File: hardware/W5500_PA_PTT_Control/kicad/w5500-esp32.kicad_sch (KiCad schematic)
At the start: 22 parts, among them J1 ESP32_DevKitC_Socket_40P_25.4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, J2 DC_IN_13V8, J5 Power, J6 PTT_ON, Q1 2SC1815, Q3 2SC1815, Q5 2SJ334, U1 TA48033S, U2 L7805

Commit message: W5500 PA/PTT制御基板の回路図でR8を1kから100に変更
Co-Authored-By: Claude Opus 5.5 <noreply@anthropic.com>
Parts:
- R8: value 1k -> 100
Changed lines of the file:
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@@
 			)
 		)
-		(property "Value" "1k"
+		(property "Value" "100"
 			(at 313.69 63.5 90)
 			(show_name no)

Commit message: W5500制御基板: R8を1kΩに、R12(Q1ベースのプルダウン)追加、Q5の足番号修正、放熱器を追加
- R8(Q5ゲートのプルアップ)を100Ωから1kΩ(1/2W推奨)へ。Q1 ON中の電流を約12〜14mAに抑える
- Q1のベースをGNDへプルダウンするR12(10kΩ)を追加(GPIO26が確定しない間もQ1をOFFに保つ)
- Q5のシンボルを端子番号1=G・2=D・3=Sのproject_symbols:2SJ334に変更
  (従来のDevice:Q_PMOSは端子番号D/G/Sで、基板データ上Q5が未接続になっていた)
- U1・U2・Q5に放熱器(秋月[105054] 20×20×25mm)。基板データでTO-220の3部品を25mm間隔に配置
- 仕様書(Rev.2.4)・接続一覧(日英・Word・PDF)、回路図PDF/SVGを更新
- ERCの件数は変更前と同じ(15件)。DRCの回路図一致チェックでR8の値とQ5のパッド未接続が解消

Co-Authored-By: Claude Opus 5.5 <noreply@anthropic.com>
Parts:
- added R12: 10k, Resistor_THT:R_Axial_DIN0207_L6.3mm_D2.5mm_P5.08mm_Vertical, symbol Device:R
- Q5: symbol Device:Q_PMOS -> project_symbols:2SJ334
- R8: value 100 -> 1k
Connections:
- net +12V: now also Q5.3 (S); no longer Q5.S
- net Power: now also Q5.2 (D); no longer Q5.D
- net at Q1.2 (C), R8.1: now also Q5.1 (G); no longer Q5.G
- net at Q1.3 (B), R6.2: now also R12.1
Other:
- note added: "U2: 13.8V(+12V)を5VへLDO変換(L7805)。発熱(13.8V-5V)*0.2A=約1.76Wのため放熱器を使用。 U1: 上記5VをさらにW5500(A1)専用の+3V3_Aへ変換(TA48033S)。発熱(5V-3.3V)*0.2A=約0.34W。放熱器を使用。 放熱器: U1・U2・Q5とも秋月[105054] 20×20×25mm(20PB020-01025、15.8℃/W)。 ESP32側(J1の3V3、DevKitC基板のオンボードLDO経由)とは完全に独立した系統。"
- note removed: "U2: 13.8V(+12V)を5VへLDO変換(L7805)。発熱(13.8V-5V)*0.2A=約1.76Wのためヒートシンク推奨。 U1: 上記5VをさらにW5500(A1)専用の+3V3_Aへ変換(TA48033S)。発熱(5V-3.3V)*0.2A=約0.34W。 ESP32側(J1の3V3、DevKitC基板のオンボードLDO経由)とは完全に独立した系統。"
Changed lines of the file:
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@@
 		)
 	)
-	(text "U2: 13.8V(+12V)を5VへLDO変換(L7805)。発熱(13.8V-5V)*0.2A=約1.76Wのためヒートシンク推奨。\nU1: 上記5VをさらにW5500(A1)専用の+3V3_Aへ変換(TA48033S)。発熱(5V-3.3V)*0.2A=約0.34W。\nESP32側(J1の3V3、DevKitC基板のオンボードLDO経由)とは完全に独立した系統。"
+	(text "U2: 13.8V(+12V)を5VへLDO変換(L7805)。発熱(13.8V-5V)*0.2A=約1.76Wのため放熱器を使用。\nU1: 上記5VをさらにW5500(A1)専用の+3V3_Aへ変換(TA48033S)。発熱(5V-3.3V)*0.2A=約0.34W。放熱器を使用。\n放熱器: U1・U2・Q5とも秋月[105054] 20×20×25mm(20PB020-01025、15.8℃/W)。\nESP32側(J1の3V3、DevKitC基板のオンボードLDO経由)とは完全に独立した系統。"
 		(exclude_from_sim no)
 		(at 256.794 139.954 0)
@@
 	)
 	(symbol
-		(lib_id "Device:Q_PMOS")
+		(lib_id "project_symbols:2SJ334")
 		(at 322.58 58.42 270)
 		(mirror x)
@@
 			)
 		)
-		(pin "D"
+		(pin "2"
 		)
-		(pin "G"
+		(pin "1"
 		)
-		(pin "S"
+		(pin "3"
 		)
 		(instances
@@
 			)
 		)
-		(property "Value" "100"
+		(property "Value" "1k"
 			(at 313.69 63.5 90)
 			(show_name no)
@@
 					(unit 1)
 				)
+			)
+		)
+	)
+	(wire
+		(pts
+			(xy 309.88 90.17) (xy 309.88 91.44)
+		)
+		(stroke
+			(width 0)
+			(type default)
+		)
+	)
+	(junction
+		(at 309.88 90.17)
+		(diameter 0)
+		(color 0 0 0 0)
+	)
+	(symbol
+		(lib_id "Device:R")
+		(at 309.88 95.25 0)
+		(unit 1)
+		(body_style 1)
+		(exclude_from_sim no)
+		(in_bom yes)
+		(on_board yes)
+		(in_pos_files yes)
+		(dnp no)
+		(property "Reference" "R12"
+			(at 311.912 94.0 0)
+			(show_name no)
+			(do_not_autoplace no)
+			(effects
+				(font
+					(size 1.27 1.27)
+				)
+			)
+		)
+		(property "Value" "10k"
+			(at 311.912 96.52 0)
+			(show_name no)
+			(do_not_autoplace no)
+			(effects
+				(font
+					(size 1.27 1.27)
+				)
+			)
+		)
+		(property "Footprint" "Resistor_THT:R_Axial_DIN0207_L6.3mm_D2.5mm_P5.08mm_Vertical"
+			(at 308.102 95.25 90)
+			(hide yes)
+			(show_name yes)
+			(do_not_autoplace no)
+			(effects
+				(font
+					(size 1.27 1.27)
+				)
+			)
+		)
+		(property "Datasheet" ""
+			(at 309.88 95.25 0)
+			(hide yes)
+			(show_name yes)
+			(do_not_autoplace no)
+			(effects
+				(font
+					(size 1.27 1.27)
+				)
+			)
+		)
+		(property "Description" ""
+			(at 309.88 95.25 0)
+			(hide yes)
+			(show_name yes)
+			(do_not_autoplace no)
+			(effects
+				(font
+					(size 1.27 1.27)
+				)
+			)
+		)
+		(pin "1"
+		)
+		(pin "2"
+		)
+		(instances
+			(project "w5500-esp32"
+				(path "/0100d23c-65ba-4b48-9527-fff8f2d69db1"
+					(reference "R12")
+					(unit 1)
+				)
+			)
+		)
+	)
+	(symbol
+		(lib_id "power:GND")
+		(at 309.88 99.06 0)
+		(unit 1)
+		(body_style 1)
+		(exclude_from_sim no)
+		(in_bom yes)
+		(on_board yes)
+		(in_pos_files yes)
+		(dnp no)
+		(fields_autoplaced yes)
+		(property "Reference" "#PWR0301"
+			(at 309.88 105.41 0)
+			(hide yes)
+			(show_name yes)
+			(do_not_autoplace no)
+			(effects
+				(font
+					(size 1.27 1.27)
+				)
+			)
+		)
+		(property "Value" ""
+			(at 322.58 102.87 0)
+			(show_name no)
+			(do_not_autoplace no)
+			(effects
+				(font
+					(size 1.27 1.27)
+				)
+			)
+		)
+		(property "Footprint" ""
+			(at 322.58 97.79 0)
+			(hide yes)
+			(show_name yes)
+			(do_not_autoplace no)
+			(effects
+				(font
+					(size 1.27 1.27)
+				)
+			)
+		)
+		(property "Datasheet" ""
+			(at 322.58 97.79 0)
+			(hide yes)
+			(show_name yes)
+			(do_not_autoplace no)
+			(effects
+				(font
+					(size 1.27 1.27)
+				)
+			)
+		)
+		(property "Description" "Power symbol creates a global label with name \"GND\" , ground"
+			(at 322.58 97.79 0)
+			(hide yes)
+			(show_name yes)
+			(do_not_autoplace no)
+			(effects
+				(font
+					(size 1.27 1.27)
+				)
+			)
+		)
+		(pin "1"
+		)
+		(instances
+			(project "w5500-esp32"
+				(path "/0100d23c-65ba-4b48-9527-fff8f2d69db1"
+					(reference "#PWR0301")
+					(unit 1)
+				)

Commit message: W5500とDevKitCのフットプリントを実物の資料に合わせて修正し、ケースの開口に合わせて配置
- A1(W5500 Lite): USR-ES1データシートに合わせ、ピン列間隔を15.24→20.32mm、7〜12番をRJ45側から数える順に修正
  (従来は右列の信号が逆につながる配置だった)。新フットプリントW5500_Lite_USR-ES1_2x06_P2.54mm_20.32mm
- J1(DevKitCソケット): Freenove公式ピン配置図に合わせ、ピンの並びを上下反転(1番5V・21番GNDがUSB-C側)。
  従来は鏡像の並びで、5Vが3V3/GNDのピンにつながる配置だった
- RJ45をケース前面の角穴(基板x=122)、USB-Cを背面の角丸穴(x=126)に合わせて配置
- 接続一覧(日英・Word・PDF)に修正内容を追記、回路図PDF/SVGを再出力。DRC違反0件

Co-Authored-By: Claude Opus 5.5 <noreply@anthropic.com>
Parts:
- A1: footprint project_footprints:W5500_Lite_2x06_P2.54mm_15.24mm -> project_footprints:W5500_Lite_USR-ES1_2x06_P2.54mm_20.32mm
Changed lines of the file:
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@@
 			)
 		)
-		(property "Footprint" "project_footprints:W5500_Lite_2x06_P2.54mm_15.24mm"
+		(property "Footprint" "project_footprints:W5500_Lite_USR-ES1_2x06_P2.54mm_20.32mm"
 			(at 106.68 68.58 0)
 			(hide yes)

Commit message: J2(+12V入力)・J5(12V出力)・J6(PTT出力)を電線はんだ付け用パッドとして配置
- ケースの丸型コネクタ(WTN-11-1253 8P)へ電線でつなぐ前提で、回路図にフットプリントを指定
  (J2・J5: Connector_Wire SolderWire-1sqmm、J6: SolderWire-0.5sqmm)
- J2は前面の丸型コネクタ側(右上)、J5・J6は背面の丸型コネクタ側(右下)に配置
- 「フットプリントが見つからない」3件を解消。DRC違反0件、ERCは変更前と同じ15件
- 仕様書(日英・Word・PDF)の配置説明を更新、回路図PDF/SVGを再出力

Co-Authored-By: Claude Opus 5.5 <noreply@anthropic.com>
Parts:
- J2, J5: footprint (none) -> Connector_Wire:SolderWire-1sqmm_1x02_P5.4mm_D1.4mm_OD2.7mm
- J6: footprint (none) -> Connector_Wire:SolderWire-0.5sqmm_1x02_P4.6mm_D0.9mm_OD2.1mm
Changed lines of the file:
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@@
 			)
 		)
-		(property "Footprint" ""
+		(property "Footprint" "Connector_Wire:SolderWire-1sqmm_1x02_P5.4mm_D1.4mm_OD2.7mm"
 			(at 142.875 171.45 0)
 			(hide yes)
@@
 			)
 		)
-		(property "Footprint" ""
+		(property "Footprint" "Connector_Wire:SolderWire-1sqmm_1x02_P5.4mm_D1.4mm_OD2.7mm"
 			(at 374.65 92.71 0)
 			(hide yes)
@@
 			)
 		)
-		(property "Footprint" ""
+		(property "Footprint" "Connector_Wire:SolderWire-0.5sqmm_1x02_P4.6mm_D0.9mm_OD2.1mm"
 			(at 374.65 113.03 0)
 			(hide yes)

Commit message: W5500制御基板: 自動配線・12V系統強化・外付けLED/XHコネクタ化と総点検の修正
- 回路図のGND記号の値が空で別ネットになっていたのを修正
- 内層をGND・+12Vの全面ベタにし、12V出力(/Power)を表裏4mmで配線、残りをFreeroutingで自動配線
- Q1/Q3を2.54mmピッチのTO-92に、R8を1/2W抵抗用フットプリントに変更
- D1/D2を外付けにしてJ7/J8で接続、J6/J7/J8をJST XH(B2B-XH-A)に変更
- C2をTA48033Sデータシートどおり33µF、C1/C3を0.33µFに変更
- Q3ベースにプルダウンR13(10k)を追加、J1のGNDピン21〜24・40を接続
- 仕様書・接続一覧(日英)を更新しWord/PDF・回路図PDF/SVGを再生成

Co-Authored-By: Claude Opus 5.5 <noreply@anthropic.com>
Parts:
- removed D1: LED_Red_3mm, LED_THT:LED_D3.0mm, symbol Device:LED
- removed D2: LED_Green_3mm, LED_THT:LED_D3.0mm, symbol Device:LED
- added J7: LED_PWR, Connector_JST:JST_XH_B2B-XH-A_1x02_P2.50mm_Vertical, symbol Connector_Generic:Conn_01x02
- added J8: LED_12V, Connector_JST:JST_XH_B2B-XH-A_1x02_P2.50mm_Vertical, symbol Connector_Generic:Conn_01x02
- added R13: 10k, Resistor_THT:R_Axial_DIN0207_L6.3mm_D2.5mm_P5.08mm_Vertical, symbol Device:R
- C1, C3: value 0.1uF -> 0.33uF
- C2: value 0.1uF -> 33uF
- J6: footprint Connector_Wire:SolderWire-0.5sqmm_1x02_P4.6mm_D0.9mm_OD2.1mm -> Connector_JST:JST_XH_B2B-XH-A_1x02_P2.50mm_Vertical
- Q1, Q3: footprint Package_TO_SOT_THT:TO-92_Inline -> Package_TO_SOT_THT:TO-92_Inline_Wide
- R8: footprint Resistor_THT:R_Axial_DIN0207_L6.3mm_D2.5mm_P5.08mm_Vertical -> Resistor_THT:R_Axial_DIN0309_L9.0mm_D3.2mm_P5.08mm_Vertical
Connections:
- net GND: now also C1.2, C2.2, J1.21 (GND), J1.22 (GND), J1.23 (GND), J1.24 (GND), J1.40 (GND), J1.7 (GND), J2.2 (Pin_2), J5.2 (Pin_2), MCU1.7 (GND), Q1.1 (E), Q3.1 (E), R12.2, U1.3 (GND), U2.2 (GND), J7.2 (Pin_2), J8.2 (Pin_2), R13.2
- net at R11.2: now also J8.1 (Pin_1)
- net at R10.2: now also J7.1 (Pin_1)
- net at Q3.3 (B), R7.2: now also R13.1
- no-connect marks 60 -> 55

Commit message: W5500制御基板: +5Vを信号線から離し、J1のピン間に配線を通さないよう再配線、J1の12番ピンを未接続に
- J1の35番ピン(W5500 RST)の配線が+5Vのビアに0.3mmまで近づいていたため、+5V(/+5v0)を
  ネットクラスSupply5V(間隔0.5mm、線幅0.6mm)に分けて再配線した。C1自身の足の間(0.4mm)だけは
  w5500-esp32.kicad_druの例外ルールで0.25mmとする。
- はんだブリッジを避けるため、J1のピンとピンの間に表裏とも配線禁止領域を置いた
  (同じ+5Vの1番・2番の間を除く)。ピン間を突き抜ける配線は0本。
- 回路図でJ1の12番ピン(GPIO25)を未接続(×)にし、MCU1に残っていたGPIO25_LNAラベルを削除した。
- DRC違反0・未配線0。ガーバー・ドリル(スルーホール103穴、ビア4)、回路図PDF/SVG、仕様書・接続一覧を更新した。

Co-Authored-By: Claude Opus 5.5 <noreply@anthropic.com>
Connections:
- net GPIO25_LNA: no longer names the net of MCU1.12 (GPIO25)
- no-connect marks 55 -> 57
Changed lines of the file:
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@@
+	)
+	(no_connect
+		(at 195.58 92.71)
+	)
+	(no_connect
+		(at 64.77 213.36)
 	)
 	(no_connect
@@
 		(pts
 			(xy 295.91 55.88) (xy 307.34 55.88)
-		)
-		(stroke
-			(width 0)
-			(type default)
-		)
-	)
-	(wire
-		(pts
-			(xy 64.77 213.36) (xy 49.53 213.36)
 		)
 		(stroke
@@
 		(effects
 			(font
-				(size 1.27 1.27)
-			)
-		)
-	)
-	(label "GPIO25_LNA"
-		(at 49.53 213.36 0)
-		(effects
-			(font

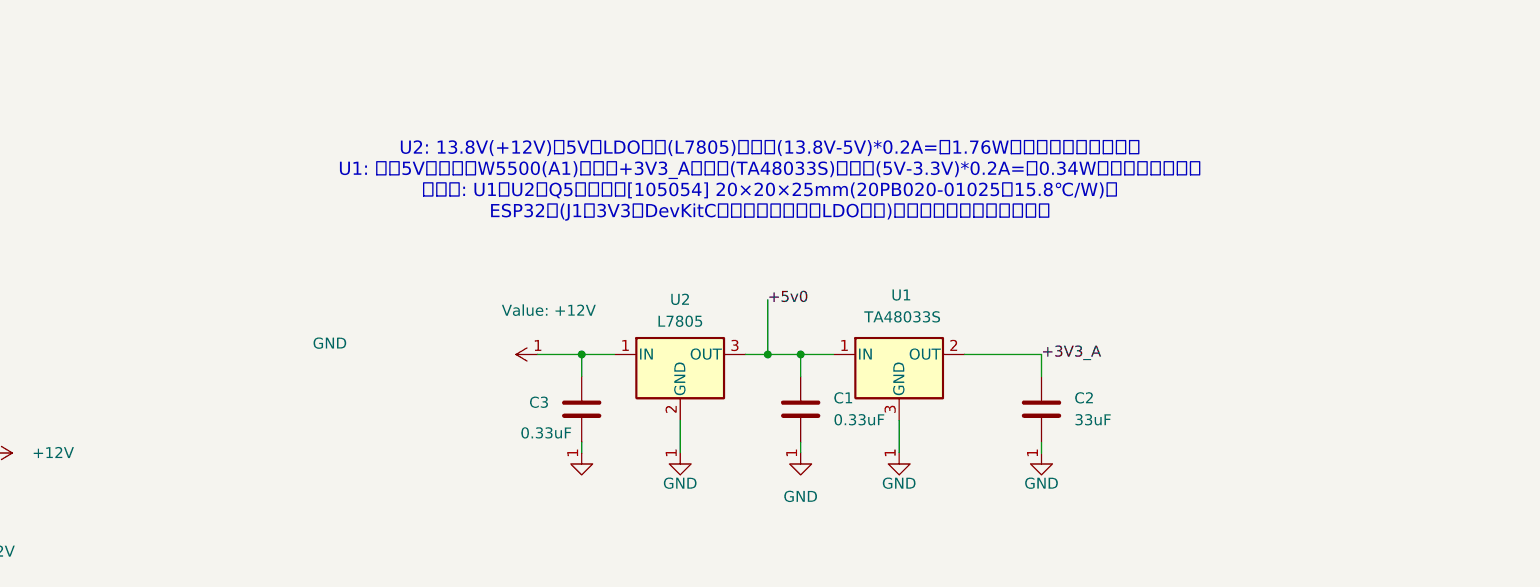
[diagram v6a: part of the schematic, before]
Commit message: W5500制御基板 Rev.1.2: 3.3VレギュレータU1をLM2940T-3.3に変更
- U1をTA48033SからLM2940T-3.3(TO-220、1=IN・2=GND・3=OUT)に変更。足の並びが違うため
  U1の2番をGND、3番を+3V3_Aにつなぎ替え、裏面の+3V3_Aの配線を引き直してベタを再充填
- C1をLM2940のデータシートどおり0.47µFに変更(C2の33µFは22µF以上・ESR 0.1〜1Ωの条件を満たす)
- U1のシンボルをproject_symbolsに追加。DRC違反0・未接続0
- シルクの版数をRev.1.2、仕様書をRev.2.8にし、版数の対応表・接続一覧を更新
- ガーバー・ドリル・ZIP・BOM・README、回路図PDF/SVG、実装図PDF、基板レイアウト画像、3D上面画像を更新

Co-Authored-By: Claude Opus 5.5 <noreply@anthropic.com>
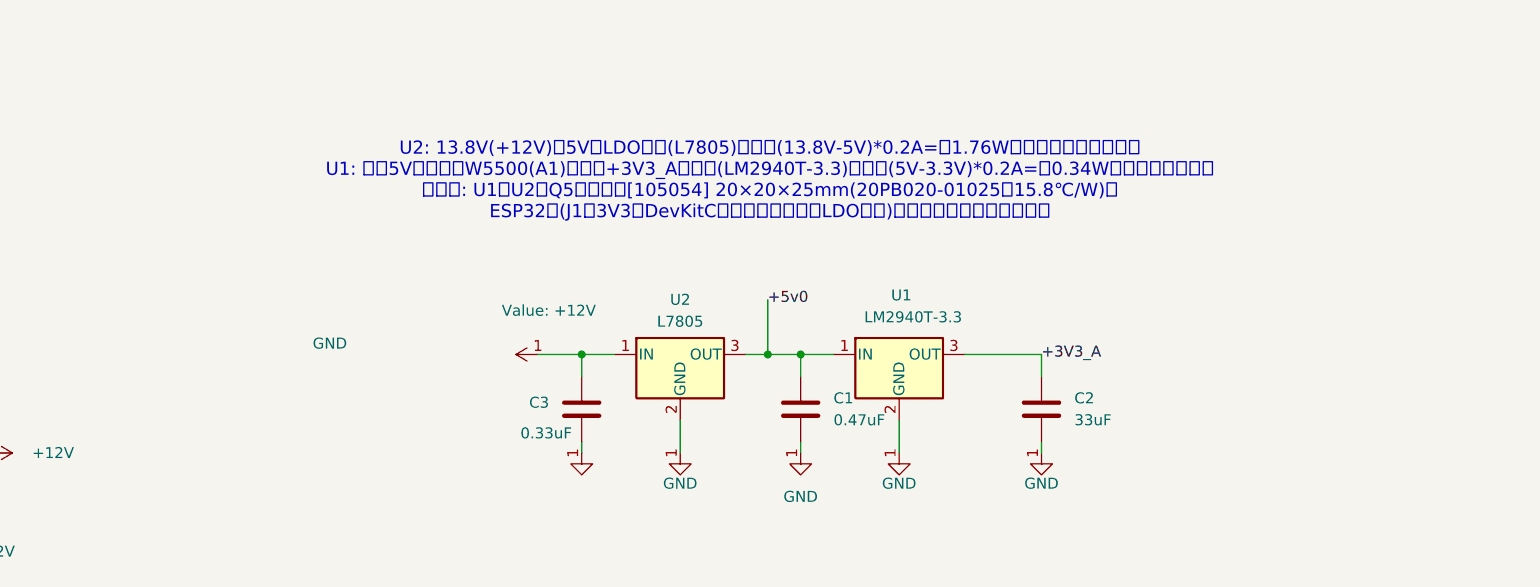
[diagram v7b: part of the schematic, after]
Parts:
- C1: value 0.33uF -> 0.47uF
- U1: value TA48033S -> LM2940T-3.3; symbol Regulator_Linear:TA48033S -> project_symbols:LM2940T-3.3
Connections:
- net +3V3_A: now also U1.3 (OUT); no longer U1.2 (OUT)
- net GND: now also U1.2 (GND); no longer U1.3 (GND)
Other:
- note added: "U2: 13.8V(+12V)を5VへLDO変換(L7805)。発熱(13.8V-5V)*0.2A=約1.76Wのため放熱器を使用。 U1: 上記5VをさらにW5500(A1)専用の+3V3_Aへ変換(LM2940T-3.3)。発熱(5V-3.3V)*0.2A=約0.34W。放熱器を使用。 放熱器: U1・U2・Q5とも秋月[105054] 20×20×25mm(20PB020-01025、15.8℃/W)。 ESP32側(J1の3V3、DevKitC基板のオンボードLDO経由)とは完全に独立した系統。"
- note removed: "U2: 13.8V(+12V)を5VへLDO変換(L7805)。発熱(13.8V-5V)*0.2A=約1.76Wのため放熱器を使用。 U1: 上記5VをさらにW5500(A1)専用の+3V3_Aへ変換(TA48033S)。発熱(5V-3.3V)*0.2A=約0.34W。放熱器を使用。 放熱器: U1・U2・Q5とも秋月[105054] 20×20×25mm(20PB020-01025、15.8℃/W)。 ESP32側(J1の3V3、DevKitC基板のオンボードLDO経由)とは完全に独立した系統。"
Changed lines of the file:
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@@
 		)
 	)
-	(text "U2: 13.8V(+12V)を5VへLDO変換(L7805)。発熱(13.8V-5V)*0.2A=約1.76Wのため放熱器を使用。\nU1: 上記5VをさらにW5500(A1)専用の+3V3_Aへ変換(TA48033S)。発熱(5V-3.3V)*0.2A=約0.34W。放熱器を使用。\n放熱器: U1・U2・Q5とも秋月[105054] 20×20×25mm(20PB020-01025、15.8℃/W)。\nESP32側(J1の3V3、DevKitC基板のオンボードLDO経由)とは完全に独立した系統。"
+	(text "U2: 13.8V(+12V)を5VへLDO変換(L7805)。発熱(13.8V-5V)*0.2A=約1.76Wのため放熱器を使用。\nU1: 上記5VをさらにW5500(A1)専用の+3V3_Aへ変換(LM2940T-3.3)。発熱(5V-3.3V)*0.2A=約0.34W。放熱器を使用。\n放熱器: U1・U2・Q5とも秋月[105054] 20×20×25mm(20PB020-01025、15.8℃/W)。\nESP32側(J1の3V3、DevKitC基板のオンボードLDO経由)とは完全に独立した系統。"
 		(exclude_from_sim no)
 		(at 256.794 139.954 0)
@@
 	)
 	(symbol
-		(lib_id "Regulator_Linear:TA48033S")
+		(lib_id "project_symbols:LM2940T-3.3")
 		(at 271.78 160.02 0)
 		(unit 1)
@@
 			)
 		)
-		(property "Value" "TA48033S"
+		(property "Value" "LM2940T-3.3"
 			(at 267.716 155.702 0)
 			(show_name no)
@@
 			)
 		)
-		(property "Datasheet" "https://akizukidenshi.com/catalog/g/g100534/"
+		(property "Datasheet" "https://www.ti.com/lit/ds/symlink/lm2940-n.pdf"
 			(at 271.78 158.73 0)
 			(hide yes)
@@
 			)
 		)
-		(property "Description" "Low dropout 3-terminal positive regulator, 3.3V 1A. IN=+12V(13.8V), OUT=+3V3_A (W5500 only). Pinout 1=IN 2=OUT 3=GND. Heatsink required (~2.1W dissipation)."
+		(property "Description" "Low dropout 3-terminal positive regulator, 3.3V 1A. IN=+5V (U2 output), OUT=+3V3_A (W5500 only). Pinout 1=IN 2=GND 3=OUT. Heatsink attached."
 			(at 271.78 160.02 0)
 			(hide yes)
@@
 			)
 		)
-		(property "Value" "0.33uF"
+		(property "Value" "0.47uF"
 			(at 264.16 167.6399 0)
 			(show_name no)
@@
 			)
 		)
-		(property "Description" "U2 output / U1 input capacitor (TA48033S datasheet: CIN=0.33uF), 16V or higher"
+		(property "Description" "U2 output / U1 input capacitor (LM2940 datasheet: CIN=0.47uF), 16V or higher"
 			(at 260.35 166.37 0)
 			(hide yes)
@@
 			)
 		)
-		(property "Description" "U1 output capacitor, electrolytic 33uF 10V or higher (TA48033S datasheet standard circuit: COUT=33uF; required for LDO stability)"
+		(property "Description" "U1 output capacitor, electrolytic 33uF 10V or higher (LM2940 datasheet: COUT>=22uF, ESR 0.1-1 ohm; required for LDO stability)"
 			(at 288.29 166.37 0)
 			(hide yes)
